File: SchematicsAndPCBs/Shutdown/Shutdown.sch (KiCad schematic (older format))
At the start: 31 parts, among them K1 3PoleSwitchingRelay, K2 3PoleSwitchingRelay, K3 DPST, K4 SPST-NO (Precharge), K5 SPST-NO (AIR), K6 SPST-NO (AIR), K7 SPST-NC (Discharge), SW1 GLVMS, SW2 SideMounted (BRB), SW3 SideMounted (BRB), SW4 Brake Over-Travel, SW5 IMBReset, SW6 BLSReset, SW7 Cockpit Shutdown (BRB), SW8 TSMS

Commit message: Updated Date
Updated date for shutdown schematic to today's date
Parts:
- BT1: symbol Device:Battery_Cell -> Shutdown-rescue:Battery_Cell-Device
- BT2: symbol Device:Battery -> Shutdown-rescue:Battery-Device
- D1, D2: symbol Diode:1N4001 -> Shutdown-rescue:1N4001-Diode
- D3, D4: symbol Device:LED -> Shutdown-rescue:LED-Device
- F1, F2, F3, F4, F5, F6, F7, F8: symbol Device:Fuse -> Shutdown-rescue:Fuse-Device
- K3: symbol Relay:G5Q-1 -> Shutdown-rescue:G5Q-1-Relay
- K4, K5, K6: symbol Relay:G5Q-1A -> Shutdown-rescue:G5Q-1A-Relay
- K7: symbol Relay:MSxx-1Bxx-75 -> Shutdown-rescue:MSxx-1Bxx-75-Relay
- R1, R2: symbol Device:R -> Shutdown-rescue:R-Device
- SW1, SW4, SW8: symbol Switch:SW_SPST -> Shutdown-rescue:SW_SPST-Switch
- SW2, SW3, SW7: symbol Switch:SW_Push_Open -> Shutdown-rescue:SW_Push_Open-Switch
- SW5, SW6: symbol Switch:SW_Push -> Shutdown-rescue:SW_Push-Switch
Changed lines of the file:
@@
 Sheet 1 1
 Title "Shutdown Circuit"
-Date "2020-05-07"
+Date "2020-09-06"
 Rev "4"
 Comp "Northeastern FSAE"
@@
 $EndDescr
 $Comp
-L power:GND #PWR?
+L Shutdown-rescue:GND-power #PWR?
 U 1 1 5D954484
 P 1800 6400
@@
 	1800 6100 1800 6250
 $Comp
-L Device:Battery_Cell BT1
+L Shutdown-rescue:Battery_Cell-Device BT1
 U 1 1 5DDBD933
 P 1800 6000
@@
 	1800 5800 1800 5550
 $Comp
-L Device:Fuse F1
+L Shutdown-rescue:Fuse-Device F1
 U 1 1 5DDBF689
 P 1800 5400
@@
 $EndComp
 $Comp
-L Switch:SW_Push_Open SW2
+L Shutdown-rescue:SW_Push_Open-Switch SW2
 U 1 1 5DDC9C70
 P 1800 4150
@@
 $EndComp
 $Comp
-L Switch:SW_Push_Open SW3
+L Shutdown-rescue:SW_Push_Open-Switch SW3
 U 1 1 5DDCB505
 P 1800 3400
@@
 $EndComp
 $Comp
-L Switch:SW_SPST SW1
+L Shutdown-rescue:SW_SPST-Switch SW1
 U 1 1 5DDCF9C3
 P 1800 4800
@@
 $EndComp
 $Comp
-L Switch:SW_Push SW5
+L Shutdown-rescue:SW_Push-Switch SW5
 U 1 1 5DDDF7AD
 P 3050 1550
@@
 Connection ~ 3350 1550
 $Comp
-L Diode:1N4001 D1
+L Shutdown-rescue:1N4001-Diode D1
 U 1 1 5DDE3BD5
 P 3900 1100
@@
 Connection ~ 4450 1100
 $Comp
-L power:GND #PWR?
+L Shutdown-rescue:GND-power #PWR?
 U 1 1 5DDEE3D1
 P 4450 1050
@@
 $EndComp
 $Comp
-L Switch:SW_Push SW6
+L Shutdown-rescue:SW_Push-Switch SW6
 U 1 1 5DE0D32A
 P 5850 1550
@@
 Connection ~ 6150 1550
 $Comp
-L Diode:1N4001 D2
+L Shutdown-rescue:1N4001-Diode D2
 U 1 1 5DE0D338
 P 6700 1100
@@
 Connection ~ 7250 1100
 $Comp
-L power:GND #PWR?
+L Shutdown-rescue:GND-power #PWR?
 U 1 1 5DE0D348
 P 7250 1050
@@
 	4700 2200 6250 2200
 $Comp
-L Device:LED D3
+L Shutdown-rescue:LED-Device D3
 U 1 1 5DE1D84D
 P 8300 1650
@@
 $EndComp
 $Comp
-L Device:LED D4
+L Shutdown-rescue:LED-Device D4
 U 1 1 5DE1EC2E
 P 8300 2050
@@
 Connection ~ 8650 1650
 $Comp
-L power:GND #PWR?
+L Shutdown-rescue:GND-power #PWR?
 U 1 1 5DE25ACA
 P 8800 1650
@@
 	9000 2300 9000 2600
 $Comp
-L Switch:SW_Push_Open SW7
+L Shutdown-rescue:SW_Push_Open-Switch SW7
 U 1 1 5DE273AC
 P 9000 2800
@@
 $EndComp
 $Comp
-L Switch:SW_SPST SW8
+L Shutdown-rescue:SW_SPST-Switch SW8
 U 1 1 5DE2B1DC
 P 9000 3750
@@
 	1800 5000 1800 5250
 $Comp
-L Relay:G5Q-1 K3
+L Shutdown-rescue:G5Q-1-Relay K3
 U 1 1 5DE3787E
 P 6100 4750
@@
 $EndComp
 $Comp
-L Relay:G5Q-1A K4
+L Shutdown-rescue:G5Q-1A-Relay K4
 U 1 1 5DE3DEF2
 P 4650 4400
@@
 $EndComp
 $Comp
-L Relay:G5Q-1A K5
+L Shutdown-rescue:G5Q-1A-Relay K5
 U 1 1 5DE454B3
 P 4650 5450
@@
 Connection ~ 4100 4600
 $Comp
-L Relay:G5Q-1A K6
+L Shutdown-rescue:G5Q-1A-Relay K6
 U 1 1 5DE60F11
 P 4650 6350
@@
 	5150 6150 5150 6100
 $Comp
-L Device:Battery BT2
+L Shutdown-rescue:Battery-Device BT2
 U 1 1 5DE6CF19
 P 5150 5900
@@
 LatchingStartStopController
 $Comp
-L Relay:MSxx-1Bxx-75 K7
+L Shutdown-rescue:MSxx-1Bxx-75-Relay K7
 U 1 1 5E4F9AAA
 P 3900 7150
@@
 	3700 7600 3300 7600
 $Comp
-L Device:R R2
+L Shutdown-rescue:R-Device R2
 U 1 1 5E50BD90
 P 3300 6550
@@
 	3500 4200 4350 4200
 $Comp
-L Device:R R1
+L Shutdown-rescue:R-Device R1
 U 1 1 5E53702E
 P 3500 5050
@@
 	9000 4950 9400 4950
 $Comp
-L Device:Fuse F2
+L Shutdown-rescue:Fuse-Device F2
 U 1 1 5EB9BA99
 P 1400 3050
@@
 $EndComp
 $Comp
-L Device:Fuse F3
+L Shutdown-rescue:Fuse-Device F3
 U 1 1 5EBD6006
 P 1400 3350
@@
 Fusebox for \nGLV Instruments
 $Comp
-L Device:Fuse F4
+L Shutdown-rescue:Fuse-Device F4
 U 1 1 5EC4170A
 P 1400 3650
@@
 $EndComp
 $Comp
-L Device:Fuse F5
+L Shutdown-rescue:Fuse-Device F5
 U 1 1 5EC41710
 P 1400 3950
@@
 $EndComp
 $Comp
-L Device:Fuse F6
+L Shutdown-rescue:Fuse-Device F6
 U 1 1 5EC4B84C
 P 1400 4250
@@
 $EndComp
 $Comp
-L Device:Fuse F7
+L Shutdown-rescue:Fuse-Device F7
 U 1 1 5EC4B852
 P 1400 4550
@@
 	1650 2500 1200 2500
 $Comp
-L Device:Fuse F8
+L Shutdown-rescue:Fuse-Device F8
 U 1 1 5EB64294
 P 1400 2750
@@
 	950  2750 950  2200
 $Comp
-L Switch:SW_SPST SW4
+L Shutdown-rescue:SW_SPST-Switch SW4
 U 1 1 5EB81F74
 P 1400 2200

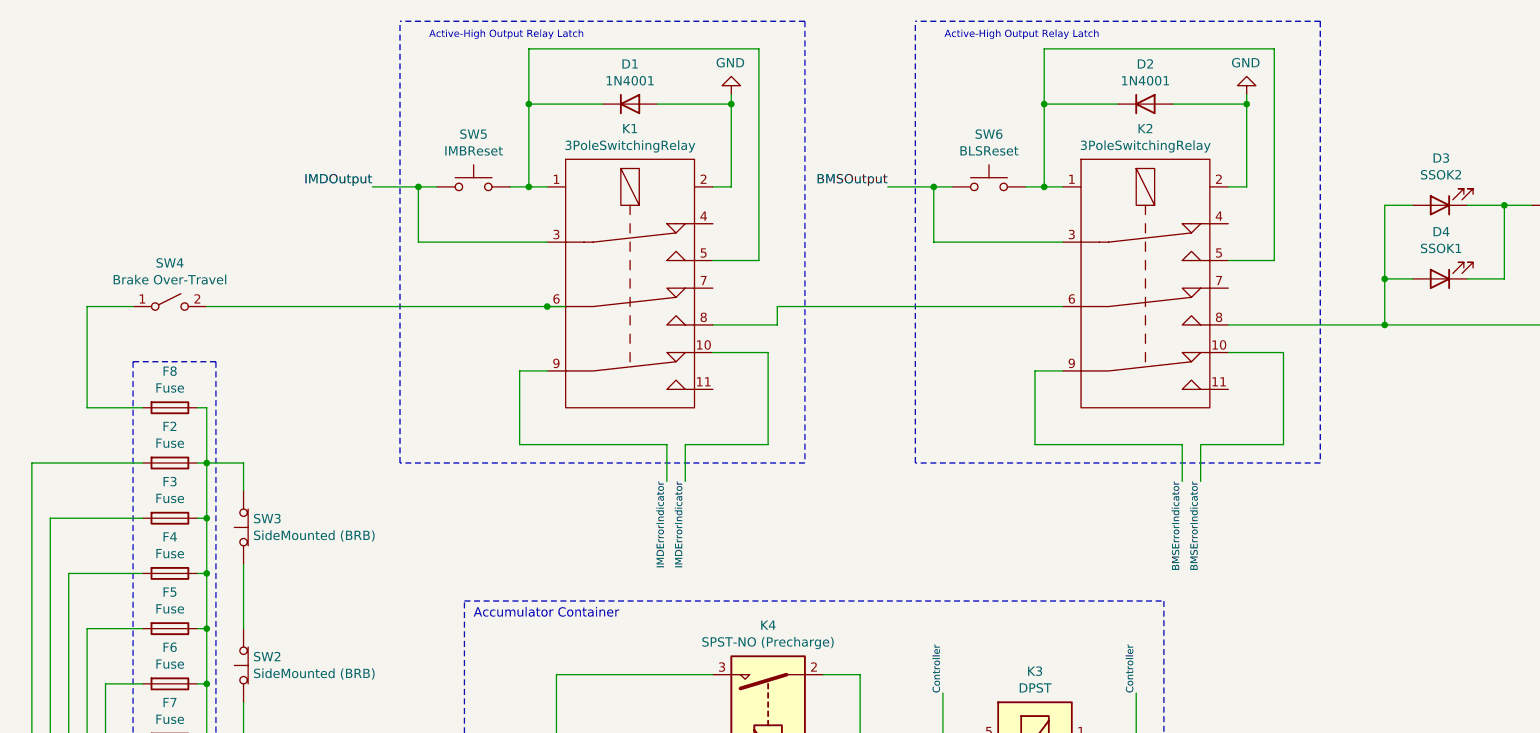
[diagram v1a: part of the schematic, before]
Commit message: Edited Shutdown Indicator wiring
Added resistors for indicators, added gnd on driver i/o side
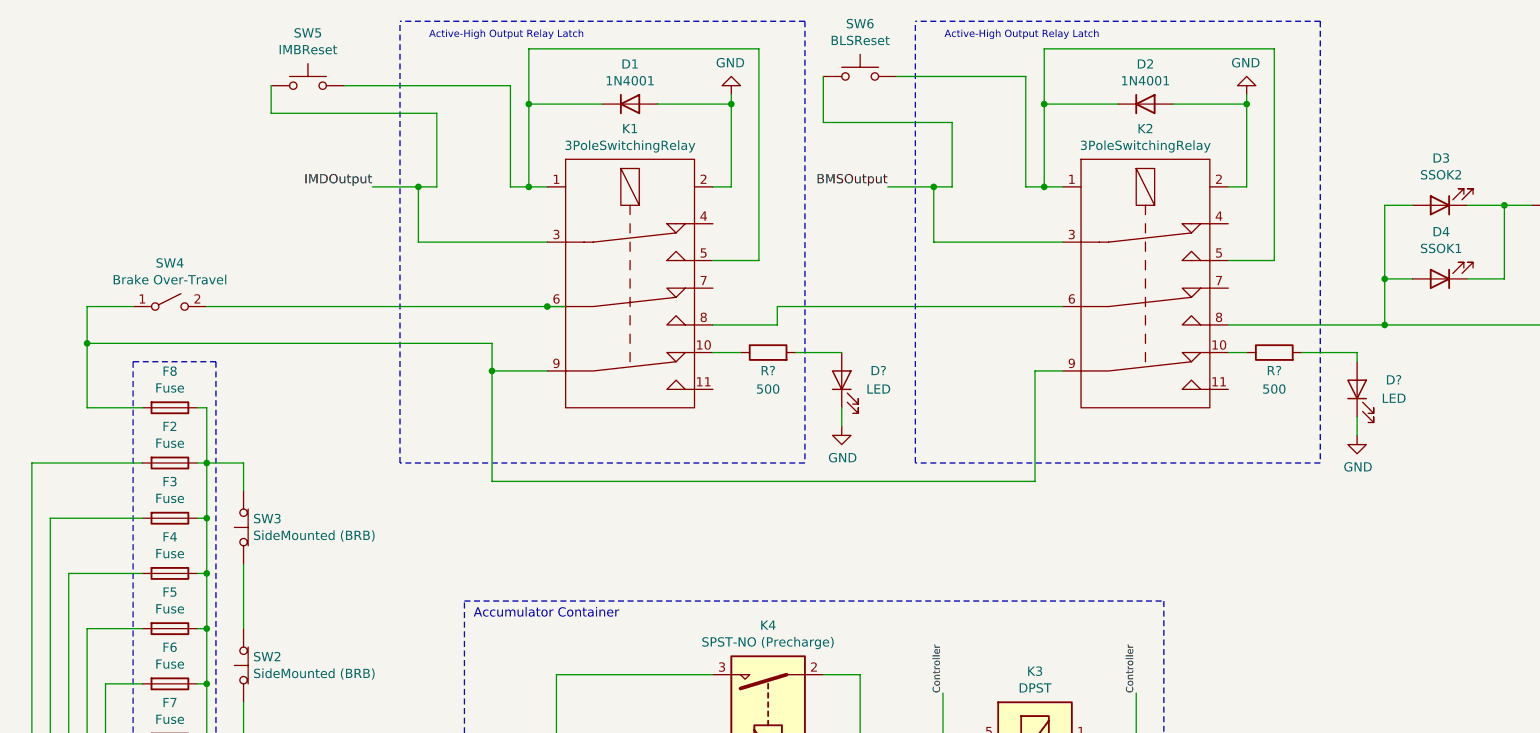
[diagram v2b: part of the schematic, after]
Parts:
- added D? (x2): LED, symbol Device:LED
- added R? (x2): 500, symbol Device:R
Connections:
- net GND: now also D?.1 (K), D?.1 (K)
- net at F8.2, SW4.1 (A): now also K1.9, K2.9
- net BMSErrorIndicator: no longer names the net of K2.10
- net BMSErrorIndicator: now also R?.1; no longer K2.9
- net IMDErrorIndicator: no longer names the net of K1.10
- net IMDErrorIndicator: now also R?.1; no longer K1.9
- new net: D?.2 (A), R?.2 (x2)
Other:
- moved on the sheet: SW5, SW6
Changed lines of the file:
@@
-$EndComp
-$Comp
-L Shutdown-rescue:3PoleSwitchingRelay-FSAE_Components K1
-U 1 1 5DDDA065
-P 3900 1350
-F 0 "K1" H 3900 1465 50  0000 C CNN
-F 1 "3PoleSwitchingRelay" H 3900 1374 50  0000 C CNN
-F 2 "" H 3900 1350 50  0001 C CNN
-F 3 "" H 3900 1350 50  0001 C CNN
-	1    3900 1350
-	1    0    0    -1
 $EndComp
 $Comp
 L Shutdown-rescue:SW_Push-Switch SW5
 U 1 1 5DDDF7AD
-P 3050 1550
-F 0 "SW5" H 3050 1835 50  0000 C CNN
-F 1 "IMBReset" H 3050 1744 50  0000 C CNN
-F 2 "" H 3050 1750 50  0001 C CNN
-F 3 "~" H 3050 1750 50  0001 C CNN
-	1    3050 1550
+P 2150 1000
+F 0 "SW5" H 2150 1285 50  0000 C CNN
+F 1 "IMBReset" H 2150 1194 50  0000 C CNN
+F 2 "" H 2150 1200 50  0001 C CNN
+F 3 "~" H 2150 1200 50  0001 C CNN
+	1    2150 1000
 	1    0    0    -1
 $EndComp
@@
 $EndComp
 Wire Wire Line
-	4350 2300 4700 2300
-Wire Wire Line
 	4700 2300 4700 2200
-Wire Wire Line
-	4350 2450 4650 2450
-Wire Wire Line
-	4650 2450 4650 2950
-Wire Wire Line
-	3450 2550 3300 2550
-Wire Wire Line
-	3300 2550 3300 2950
-Wire Wire Line
-	3300 2950 4100 2950
-Wire Wire Line
-	4100 2950 4100 3150
-Wire Wire Line
-	4650 2950 4200 2950
-Wire Wire Line
-	4200 2950 4200 3150
 Text Label 2500 1550 2    50   ~ 0
 IMDOutput
@@
 Text Notes 3650 750  2    39   ~ 0
 Active-High Output Relay Latch
-Text Label 4100 3150 3    39   ~ 0
-IMDErrorIndicator
-Text Label 4200 3150 3    39   ~ 0
-IMDErrorIndicator
 $Comp
 L Shutdown-rescue:3PoleSwitchingRelay-FSAE_Components K2
@@
 L Shutdown-rescue:SW_Push-Switch SW6
 U 1 1 5DE0D32A
-P 5850 1550
-F 0 "SW6" H 5850 1835 50  0000 C CNN
-F 1 "BLSReset" H 5850 1744 50  0000 C CNN
-F 2 "" H 5850 1750 50  0001 C CNN
-F 3 "~" H 5850 1750 50  0001 C CNN
-	1    5850 1550
+P 5150 950
+F 0 "SW6" H 5150 1235 50  0000 C CNN
+F 1 "BLSReset" H 5150 1144 50  0000 C CNN
+F 2 "" H 5150 1150 50  0001 C CNN
+F 3 "~" H 5150 1150 50  0001 C CNN
+	1    5150 950
 	1    0    0    -1
 $EndComp
@@
 $EndComp
 Wire Wire Line
-	7150 2450 7450 2450
-Wire Wire Line
-	7450 2450 7450 2950
-Wire Wire Line
 	6250 2550 6100 2550
-Wire Wire Line
-	6100 2550 6100 2950
-Wire Wire Line
-	6100 2950 6900 2950
-Wire Wire Line
-	6900 2950 6900 3150
-Wire Wire Line
-	7450 2950 7000 2950
-Wire Wire Line
-	7000 2950 7000 3150
 Text Label 5300 1550 2    50   ~ 0
 BMSOutput
@@
 Text Notes 6450 750  2    39   ~ 0
 Active-High Output Relay Latch
-Text Label 6900 3150 3    39   ~ 0
-BMSErrorIndicator
-Text Label 7000 3150 3    39   ~ 0
-BMSErrorIndicator
 Wire Wire Line
 	4700 2200 6250 2200
@@
 Wire Wire Line
 	1800 6250 1800 6400
-Wire Wire Line
-	1800 3050 1800 3200
 Text Label 1050 4950 3    39   ~ 0
 IMD
@@
 Wire Wire Line
 	2450 6250 1800 6250
-Connection ~ 3450 2200
-Wire Wire Line
-	3450 2200 3550 2200
 Wire Notes Line
 	1650 2500 1200 2500
@@
 	1250 2750 950  2750
 Wire Wire Line
-	950  2750 950  2200
+	950  2750 950  2400
 $Comp
 L Shutdown-rescue:SW_SPST-Switch SW4
@@
 $EndComp
 Wire Wire Line
+	1200 2200 950  2200
+Wire Notes Line
+	1650 2500 1650 4800
+Wire Notes Line
+	1200 2500 1200 4800
+Wire Wire Line
+	1800 3600 1800 3950
+$Comp
+L power:GND #PWR?
+U 1 1 5F5F2D04
+P 5050 2850
+F 0 "#PWR?" H 5050 2600 50  0001 C CNN
+F 1 "GND" H 5055 2677 50  0000 C CNN
+F 2 "" H 5050 2850 50  0001 C CNN
+F 3 "" H 5050 2850 50  0001 C CNN
+	1    5050 2850
+	1    0    0    -1
+$EndComp
+$Comp
+L Device:LED D?
+U 1 1 5F5FAA05
+P 5050 2600
+F 0 "D?" V 5100 2400 50  0000 C CNN
+F 1 "LED" V 5000 2400 50  0000 C CNN
+F 2 "" H 5050 2600 50  0001 C CNN
+F 3 "~" H 5050 2600 50  0001 C CNN
+	1    5050 2600
+	0    -1   -1   0
+$EndComp
+Wire Wire Line
 	1600 2200 3450 2200
 Wire Wire Line
-	1200 2200 950  2200
-Wire Notes Line
-	1650 2500 1650 4800
-Wire Notes Line
-	1200 2500 1200 4800
-Wire Wire Line
-	1800 3600 1800 3950
+	3450 2200 3550 2200
+Connection ~ 3450 2200
+$Comp
+L Shutdown-rescue:3PoleSwitchingRelay-FSAE_Components K1
+U 1 1 5DDDA065
+P 3900 1350
+F 0 "K1" H 3900 1465 50  0000 C CNN
+F 1 "3PoleSwitchingRelay" H 3900 1374 50  0000 C CNN
+F 2 "" H 3900 1350 50  0001 C CNN
+F 3 "" H 3900 1350 50  0001 C CNN
+	1    3900 1350
+	1    0    0    -1
+$EndComp
+Wire Wire Line
+	5050 2750 5050 2850
+$Comp
+L power:GND #PWR?
+U 1 1 5F6CFD49
+P 7850 2900
+F 0 "#PWR?" H 7850 2650 50  0001 C CNN
+F 1 "GND" H 7855 2727 50  0000 C CNN
+F 2 "" H 7850 2900 50  0001 C CNN
+F 3 "" H 7850 2900 50  0001 C CNN
+	1    7850 2900
+	1    0    0    -1
+$EndComp
+$Comp
+L Device:LED D?
+U 1 1 5F6CFD4F
+P 7850 2650
+F 0 "D?" V 7900 2450 50  0000 C CNN
+F 1 "LED" V 7800 2450 50  0000 C CNN
+F 2 "" H 7850 2650 50  0001 C CNN
+F 3 "~" H 7850 2650 50  0001 C CNN
+	1    7850 2650
+	0    -1   -1   0
+$EndComp
+Wire Wire Line
+	6100 2550 6100 3150
+$Comp
+L Device:R R?
+U 1 1 5F718C39
+P 4650 2450
+F 0 "R?" V 4550 2450 50  0000 C CNN
+F 1 "500" V 4450 2450 50  0000 C CNN
+F 2 "" V 4580 2450 50  0001 C CNN
+F 3 "~" H 4650 2450 50  0001 C CNN
+	1    4650 2450
+	0    -1   -1   0
+$EndComp
+Wire Wire Line
+	4350 2300 4700 2300
+Wire Wire Line
+	4500 2450 4350 2450
+Wire Wire Line
+	4800 2450 5050 2450
+$Comp
+L Device:R R?
+U 1 1 5F73B323
+P 7400 2450
+F 0 "R?" V 7300 2450 50  0000 C CNN
+F 1 "500" V 7200 2450 50  0000 C CNN
+F 2 "" V 7330 2450 50  0001 C CNN
+F 3 "~" H 7400 2450 50  0001 C CNN
+	1    7400 2450
+	0    -1   -1   0
+$EndComp
+Wire Wire Line
+	7550 2450 7850 2450
+Wire Wire Line
+	7850 2500 7850 2450
+Wire Wire Line
+	7250 2450 7150 2450
+Wire Wire Line
+	7850 2800 7850 2900
+Wire Wire Line
+	1800 3050 1800 3200
+Connection ~ 950  2400
+Wire Wire Line
+	950  2400 950  2200
+Wire Wire Line
+	3150 2400 3150 2550
+Wire Wire Line
+	3150 2550 3450 2550
+Wire Wire Line
+	950  2400 3150 2400
+Wire Wire Line
+	3150 2550 3150 3150
+Wire Wire Line
+	3150 3150 6100 3150
+Connection ~ 3150 2550
+Wire Wire Line
+	4950 950  4950 1200
+Wire Wire Line
+	4950 1200 5650 1200
+Wire Wire Line
+	5650 1200 5650 1550
+Wire Wire Line
+	5350 950  6050 950
+Wire Wire Line
+	6050 950  6050 1550
+Wire Wire Line
+	1950 1000 1950 1150
+Wire Wire Line
+	1950 1150 2850 1150
+Wire Wire Line
+	2850 1150 2850 1550
+Wire Wire Line
+	3250 1550 3250 1000
+Wire Wire Line
+	3250 1000 2350 1000
 $EndSCHEMATC

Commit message: Added numbers and fixed library
-Fixed custom parts to refer to NER lubrary
-Added numbers to the new resistors and diodes
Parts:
- K1, K2: symbol Shutdown-rescue:3PoleSwitchingRelay-FSAE_Components -> NER:3PoleSwitchingRelay
- gave numbers to parts that had none: 4
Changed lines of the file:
@@
 EESchema Schematic File Version 4
+LIBS:Shutdown-cache
 EELAYER 30 0
 EELAYER END
@@
 Active-High Output Relay Latch
 $Comp
-L Shutdown-rescue:3PoleSwitchingRelay-FSAE_Components K2
+L NER:3PoleSwitchingRelay K2
 U 1 1 5DE0D324
 P 6700 1350
@@
 $EndComp
 $Comp
-L Device:LED D?
+L Device:LED D5
 U 1 1 5F5FAA05
 P 5050 2600
-F 0 "D?" V 5100 2400 50  0000 C CNN
+F 0 "D5" V 5100 2400 50  0000 C CNN
 F 1 "LED" V 5000 2400 50  0000 C CNN
 F 2 "" H 5050 2600 50  0001 C CNN
@@
 Connection ~ 3450 2200
 $Comp
-L Shutdown-rescue:3PoleSwitchingRelay-FSAE_Components K1
+L NER:3PoleSwitchingRelay K1
 U 1 1 5DDDA065
 P 3900 1350
@@
 $EndComp
 $Comp
-L Device:LED D?
+L Device:LED D6
 U 1 1 5F6CFD4F
 P 7850 2650
-F 0 "D?" V 7900 2450 50  0000 C CNN
+F 0 "D6" V 7900 2450 50  0000 C CNN
 F 1 "LED" V 7800 2450 50  0000 C CNN
 F 2 "" H 7850 2650 50  0001 C CNN
@@
 	6100 2550 6100 3150
 $Comp
-L Device:R R?
+L Device:R R3
 U 1 1 5F718C39
 P 4650 2450
-F 0 "R?" V 4550 2450 50  0000 C CNN
+F 0 "R3" V 4550 2450 50  0000 C CNN
 F 1 "500" V 4450 2450 50  0000 C CNN
 F 2 "" V 4580 2450 50  0001 C CNN
@@
 	4800 2450 5050 2450
 $Comp
-L Device:R R?
+L Device:R R4
 U 1 1 5F73B323
 P 7400 2450
-F 0 "R?" V 7300 2450 50  0000 C CNN
+F 0 "R4" V 7300 2450 50  0000 C CNN
 F 1 "500" V 7200 2450 50  0000 C CNN
 F 2 "" V 7330 2450 50  0001 C CNN
